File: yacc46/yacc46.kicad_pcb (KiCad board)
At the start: 2 copper layers, 281.5 x 112.1 mm, 141 parts, among them J1 CX70M-24P1, J2 OLED_I2C, J3 AVR-ISP-6, J4 GLOVE_I2C, SW1 SW_PUSH, SW10 SW_PUSH, SW11 SW_PUSH, SW12 SW_PUSH, SW13 SW_PUSH, SW14 SW_PUSH, SW15 SW_PUSH, SW16 SW_PUSH, SW17 SW_PUSH, SW18 SW_PUSH, SW19 Rotary_Encoder_Switch, SW2 SW_PUSH, SW20 SW_PUSH, SW21 SW_PUSH, SW22 SW_PUSH, SW23 SW_PUSH, SW24 SW_PUSH, SW25 SW_PUSH, SW26 SW_PUSH, SW27 SW_PUSH, SW28 SW_PUSH, SW29 SW_PUSH, SW3 SW_PUSH, SW30 SW_PUSH, SW31 SW_PUSH, SW32 SW_PUSH, SW33 SW_PUSH, SW34 SW_PUSH, SW35 SW_PUSH, SW36 Rotary_Encoder_Switch, SW37 SW_PUSH, SW38 SW_PUSH, SW39 SW_PUSH, SW4 SW_PUSH, SW40 SW_PUSH, SW41 SW_PUSH, SW42 SW_PUSH, SW43 SW_PUSH, SW44 SW_PUSH, SW45 SW_PUSH, SW46 SW_PUSH, SW47 SW_Push, SW5 SW_PUSH, SW6 SW_PUSH, SW7 SW_PUSH, SW8 SW_PUSH, SW9 SW_PUSH, U1 ATmega32U4-AU, Y1 16MHz

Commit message: GND viaを追加
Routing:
- net UDN: track 213.3 -> 212.7 mm
- net UDP: track 210.6 -> 210.1 mm
- net COL5: track 265.7 -> 266.2 mm, vias 5 -> 6
- net Net-(LED10-Pad3): vias 2 -> 4
- net GND: vias 58 -> 67

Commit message: GND, USB配線を修正
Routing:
- net SDA: track 124.9 -> 181.6 mm
- net SCL: track 124.2 -> 179.8 mm
- net VBUS: track 775.5 -> 784.1 mm, vias 0 -> 5
- net UDP: track 210.1 -> 215.4 mm
- net UDN: track 212.7 -> 218.0 mm
- net GND: track 898.8 -> 893.6 mm, vias 67 -> 159
- net COL6: track 184.9 -> 188.6 mm
- net COL5: track 266.2 -> 268.6 mm
- net COL4: track 301.0 -> 303.4 mm
- net COL3: track 356.6 -> 359.0 mm
- net COL2: track 364.9 -> 367.3 mm
- net COL1: track 382.3 -> 384.7 mm
- net COL0: track 386.4 -> 388.8 mm

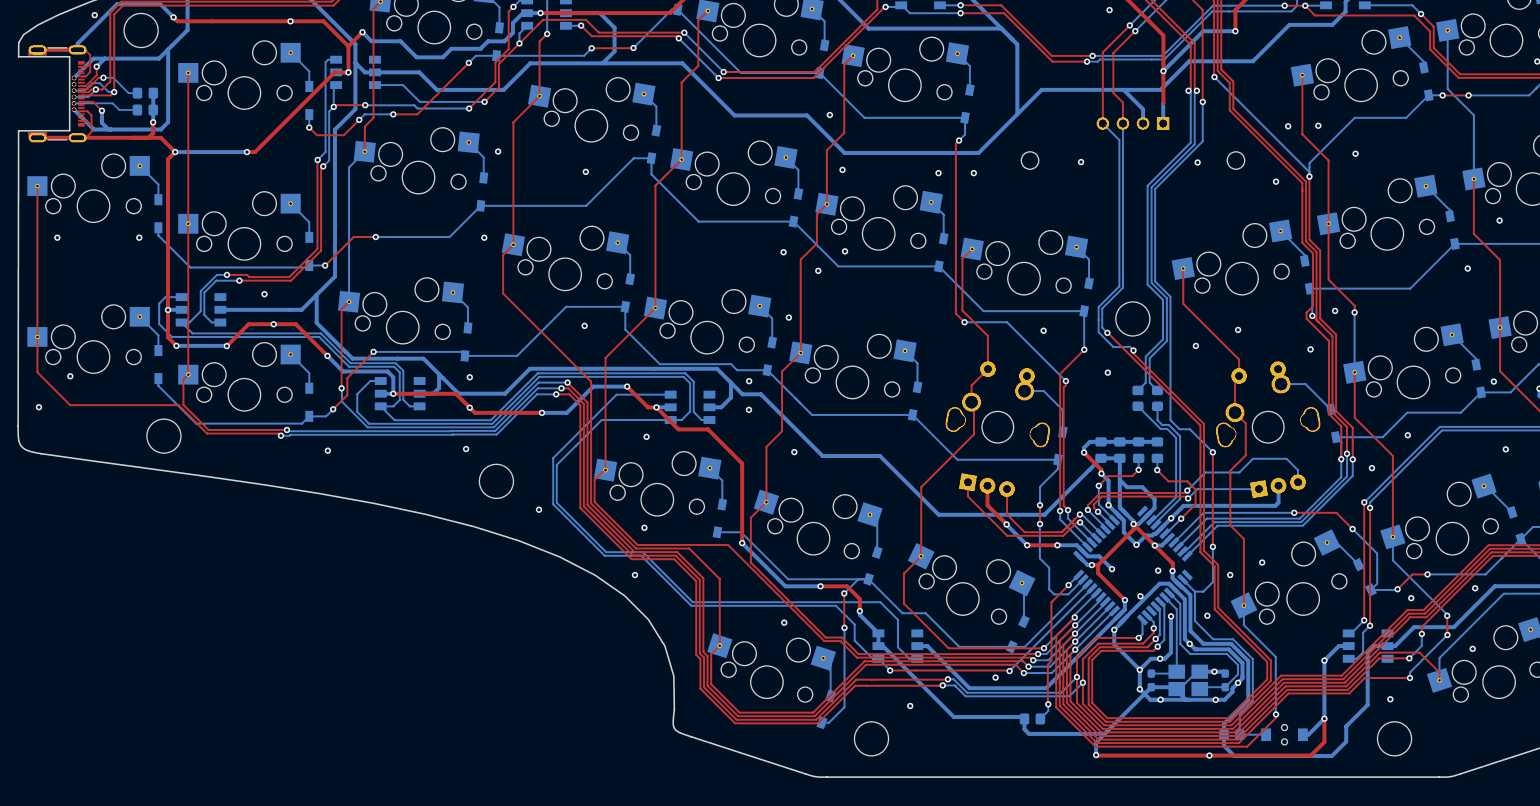
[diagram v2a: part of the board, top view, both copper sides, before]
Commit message: 基板を調整
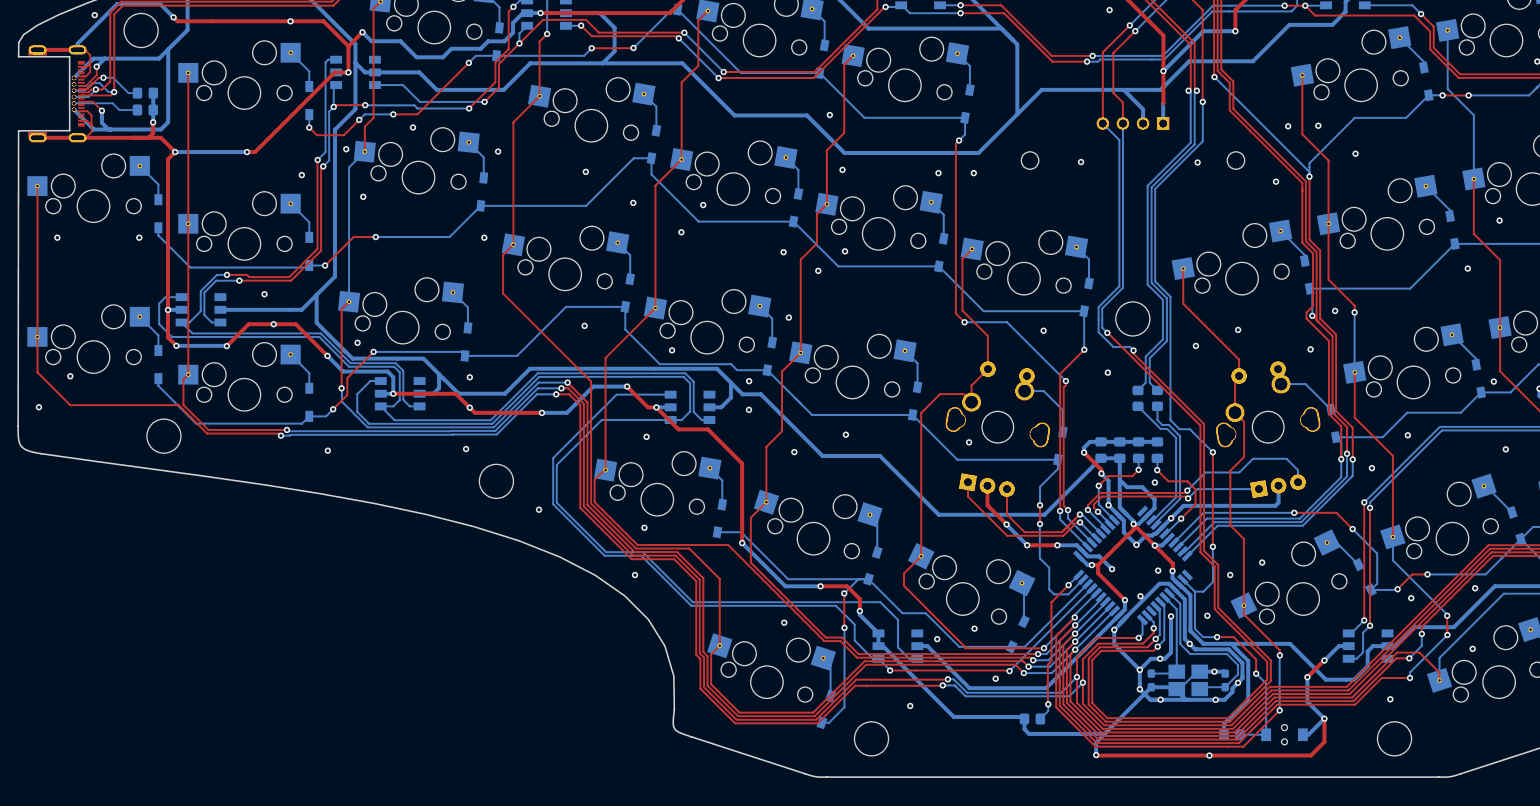
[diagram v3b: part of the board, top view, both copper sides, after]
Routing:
- net VBUS: track 784.1 -> 776.0 mm
- net COL6: track 188.6 -> 190.8 mm, vias 3 -> 4
- net GND: track 893.6 -> 895.4 mm, vias 159 -> 174
- net RESET: track 164.2 -> 165.0 mm, vias 4 -> 6
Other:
- board text added: "RESET"
- board text removed: "RST"

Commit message: v0.2発注データ
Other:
- rule pad_to_mask_clearance: 0.05 -> 0
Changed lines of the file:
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@@
     (pad_size 0.23 0.85)
     (pad_drill 0)
-    (pad_to_mask_clearance 0.05)
+    (pad_to_mask_clearance 0)
     (aux_axis_origin 0 0)
     (visible_elements 7FFFFFFF)
     (pcbplotparams
-      (layerselection 0x010fc_ffffffff)
-      (usegerberextensions false)
+      (layerselection 0x010f0_ffffffff)
+      (usegerberextensions true)
       (usegerberattributes true)
       (usegerberadvancedattributes true)
-      (creategerberjobfile true)
+      (creategerberjobfile false)
       (excludeedgelayer true)
       (linewidth 0.100000)
@@
       (outputformat 1)
       (mirror false)
-      (drillshape 1)
+      (drillshape 0)
       (scaleselection 1)
-      (outputdirectory ""))
+      (outputdirectory "garver_v0.2/"))
   )
   (net 0 "")
@@
       (effects (font (size 0.5 0.5) (thickness 0.08)) (justify mirror))
     )
-    (pad 2 smd roundrect (at 1 0) (size 1.2 1.4) (layers B.Cu B.Paste B.Mask) (roundrect_rratio 0.208333)
+    (pad 2 smd roundrect (at 1 0) (size 1.2 1.4) (layers B.Cu B.Paste B.Mask) (roundrect_rratio 0.2083325)
       (net 110 HWB))
-    (pad 1 smd roundrect (at -1 0) (size 1.2 1.4) (layers B.Cu B.Paste B.Mask) (roundrect_rratio 0.208333)
+    (pad 1 smd roundrect (at -1 0) (size 1.2 1.4) (layers B.Cu B.Paste B.Mask) (roundrect_rratio 0.2083325)
       (net 2 GND))
     (model ${KISYS3DMOD}/Resistor_SMD.3dshapes/R_0805_2012Metric.wrl
@@
       (effects (font (size 0.5 0.5) (thickness 0.08)) (justify mirror))
     )
-    (pad 2 smd roundrect (at 1 0 90) (size 1.2 1.4) (layers B.Cu B.Paste B.Mask) (roundrect_rratio 0.208333)
+    (pad 2 smd roundrect (at 1 0 90) (size 1.2 1.4) (layers B.Cu B.Paste B.Mask) (roundrect_rratio 0.2083325)
       (net 63 UDN))
-    (pad 1 smd roundrect (at -1 0 90) (size 1.2 1.4) (layers B.Cu B.Paste B.Mask) (roundrect_rratio 0.208333)
+    (pad 1 smd roundrect (at -1 0 90) (size 1.2 1.4) (layers B.Cu B.Paste B.Mask) (roundrect_rratio 0.2083325)
       (net 108 DN))
     (model ${KISYS3DMOD}/Resistor_SMD.3dshapes/R_0805_2012Metric.wrl
@@
       (effects (font (size 0.5 0.5) (thickness 0.08)) (justify mirror))
     )
-    (pad 2 smd roundrect (at 1.0375 0 270) (size 1.175 1.45) (layers B.Cu B.Paste B.Mask) (roundrect_rratio 0.212766)
+    (pad 2 smd roundrect (at 1.0375 0 270) (size 1.175 1.45) (layers B.Cu B.Paste B.Mask) (roundrect_rratio 0.2127659574468085)
       (net 1 VBUS))
-    (pad 1 smd roundrect (at -1.0375 0 270) (size 1.175 1.45) (layers B.Cu B.Paste B.Mask) (roundrect_rratio 0.212766)
+    (pad 1 smd roundrect (at -1.0375 0 270) (size 1.175 1.45) (layers B.Cu B.Paste B.Mask) (roundrect_rratio 0.2127659574468085)
       (net 2 GND))
     (model ${KISYS3DMOD}/Capacitor_SMD.3dshapes/C_0805_2012Metric.wrl
@@
       (effects (font (size 0.5 0.5) (thickness 0.08)) (justify mirror))
     )
-    (pad 1 smd roundrect (at -1.0375 0 270) (size 1.175 1.45) (layers B.Cu B.Paste B.Mask) (roundrect_rratio 0.212766)
+    (pad 1 smd roundrect (at -1.0375 0 270) (size 1.175 1.45) (layers B.Cu B.Paste B.Mask) (roundrect_rratio 0.2127659574468085)
       (net 2 GND))
-    (pad 2 smd roundrect (at 1.0375 0 270) (size 1.175 1.45) (layers B.Cu B.Paste B.Mask) (roundrect_rratio 0.212766)
+    (pad 2 smd roundrect (at 1.0375 0 270) (size 1.175 1.45) (layers B.Cu B.Paste B.Mask) (roundrect_rratio 0.2127659574468085)
       (net 1 VBUS))
     (model ${KISYS3DMOD}/Capacitor_SMD.3dshapes/C_0805_2012Metric.wrl
@@
       (effects (font (size 0.5 0.5) (thickness 0.08)) (justify mirror))
     )
-    (pad 2 smd roundrect (at 1.0375 0 90) (size 1.175 1.45) (layers B.Cu B.Paste B.Mask) (roundrect_rratio 0.212766)
+    (pad 2 smd roundrect (at 1.0375 0 90) (size 1.175 1.45) (layers B.Cu B.Paste B.Mask) (roundrect_rratio 0.2127659574468085)
       (net 2 GND))
-    (pad 1 smd roundrect (at -1.0375 0 90) (size 1.175 1.45) (layers B.Cu B.Paste B.Mask) (roundrect_rratio 0.212766)
+    (pad 1 smd roundrect (at -1.0375 0 90) (size 1.175 1.45) (layers B.Cu B.Paste B.Mask) (roundrect_rratio 0.2127659574468085)
       (net 3 AREF))
     (model ${KISYS3DMOD}/Capacitor_SMD.3dshapes/C_0805_2012Metric.wrl
@@
       (effects (font (size 0.5 0.5) (thickness 0.08)) (justify mirror))
     )
-    (pad 1 smd roundrect (at -1.0375 0 90) (size 1.175 1.45) (layers B.Cu B.Paste B.Mask) (roundrect_rratio 0.212766)
+    (pad 1 smd roundrect (at -1.0375 0 90) (size 1.175 1.45) (layers B.Cu B.Paste B.Mask) (roundrect_rratio 0.2127659574468085)
       (net 4 UCAP))
-    (pad 2 smd roundrect (at 1.0375 0 90) (size 1.175 1.45) (layers B.Cu B.Paste B.Mask) (roundrect_rratio 0.212766)
+    (pad 2 smd roundrect (at 1.0375 0 90) (size 1.175 1.45) (layers B.Cu B.Paste B.Mask) (roundrect_rratio 0.2127659574468085)
       (net 2 GND))
     (model ${KISYS3DMOD}/Capacitor_SMD.3dshapes/C_0805_2012Metric.wrl
@@
       (effects (font (size 0.5 0.5) (thickness 0.08)) (justify mirror))
     )
-    (pad 1 smd roundrect (at -1 0 180) (size 1.2 1.4) (layers B.Cu B.Paste B.Mask) (roundrect_rratio 0.208333)
+    (pad 1 smd roundrect (at -1 0 180) (size 1.2 1.4) (layers B.Cu B.Paste B.Mask) (roundrect_rratio 0.2083325)
       (net 2 GND))
-    (pad 2 smd roundrect (at 1 0 180) (size 1.2 1.4) (layers B.Cu B.Paste B.Mask) (roundrect_rratio 0.208333)
+    (pad 2 smd roundrect (at 1 0 180) (size 1.2 1.4) (layers B.Cu B.Paste B.Mask) (roundrect_rratio 0.2083325)
       (net 70 /CC1))
     (model ${KISYS3DMOD}/Resistor_SMD.3dshapes/R_0805_2012Metric.wrl
@@
       (effects (font (size 0.5 0.5) (thickness 0.08)) (justify mirror))
     )
-    (pad 2 smd roundrect (at 1 0) (size 1.2 1.4) (layers B.Cu B.Paste B.Mask) (roundrect_rratio 0.208333)
+    (pad 2 smd roundrect (at 1 0) (size 1.2 1.4) (layers B.Cu B.Paste B.Mask) (roundrect_rratio 0.2083325)
       (net 2 GND))
-    (pad 1 smd roundrect (at -1 0) (size 1.2 1.4) (layers B.Cu B.Paste B.Mask) (roundrect_rratio 0.208333)
+    (pad 1 smd roundrect (at -1 0) (size 1.2 1.4) (layers B.Cu B.Paste B.Mask) (roundrect_rratio 0.2083325)
       (net 65 /CC2))
     (model ${KISYS3DMOD}/Resistor_SMD.3dshapes/R_0805_2012Metric.wrl
@@
       (effects (font (size 0.5 0.5) (thickness 0.08)) (justify mirror))
     )
-    (pad 1 smd roundrect (at -1 0 270) (size 1.2 1.4) (layers B.Cu B.Paste B.Mask) (roundrect_rratio 0.208333)
+    (pad 1 smd roundrect (at -1 0 270) (size 1.2 1.4) (layers B.Cu B.Paste B.Mask) (roundrect_rratio 0.2083325)
       (net 64 UDP))
-    (pad 2 smd roundrect (at 1 0 270) (size 1.2 1.4) (layers B.Cu B.Paste B.Mask) (roundrect_rratio 0.208333)
+    (pad 2 smd roundrect (at 1 0 270) (size 1.2 1.4) (layers B.Cu B.Paste B.Mask) (roundrect_rratio 0.2083325)
       (net 109 DP))
     (model ${KISYS3DMOD}/Resistor_SMD.3dshapes/R_0805_2012Metric.wrl
@@
       (effects (font (size 0.5 0.5) (thickness 0.08)) (justify mirror))
     )
-    (pad 1 smd roundrect (at -1 0) (size 1.2 1.4) (layers B.Cu B.Paste B.Mask) (roundrect_rratio 0.208333)
+    (pad 1 smd roundrect (at -1 0) (size 1.2 1.4) (layers B.Cu B.Paste B.Mask) (roundrect_rratio 0.2083325)
       (net 1 VBUS))
-    (pad 2 smd roundrect (at 1 0) (size 1.2 1.4) (layers B.Cu B.Paste B.Mask) (roundrect_rratio 0.208333)
+    (pad 2 smd roundrect (at 1 0) (size 1.2 1.4) (layers B.Cu B.Paste B.Mask) (roundrect_rratio 0.2083325)
       (net 78 RESET))
     (model ${KISYS3DMOD}/Resistor_SMD.3dshapes/R_0805_2012Metric.wrl

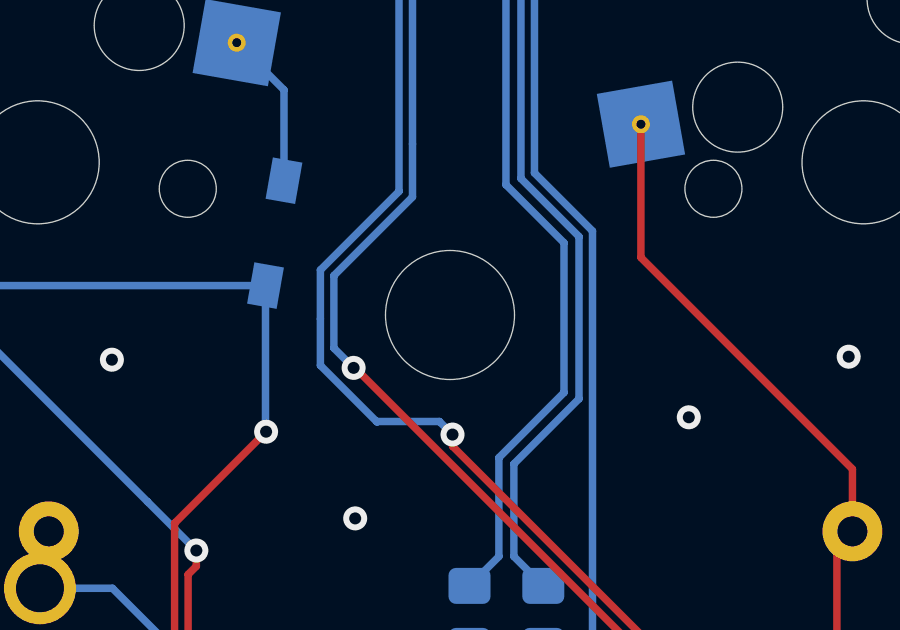
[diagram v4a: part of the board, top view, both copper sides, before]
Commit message: yacc46 PCB: MountingHoleを修正
- 中央の穴を削除
- リファレンスを修正
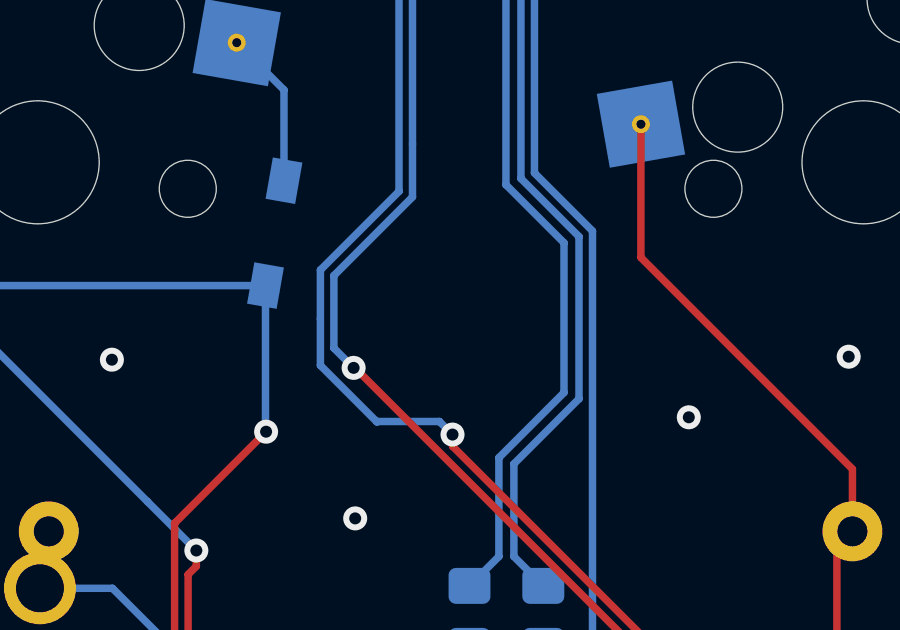
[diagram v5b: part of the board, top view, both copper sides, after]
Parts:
- removed HOLE13: Val**, foostan_kbd:M2_HOLE_v2
- renumbered HOLE1 to H1, HOLE10 to H10, HOLE11 to H11, HOLE12 to H12, HOLE14 to H13, HOLE15 to H14, HOLE2 to H2, HOLE3 to H3, HOLE4 to H4, HOLE5 to H5, HOLE6 to H6, HOLE7 to H7, HOLE8 to H8, HOLE9 to H9

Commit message: [WIP]仮配置
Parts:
- added D47: PRTR5V0U2X, 1m38_kbd:PRTR5V0U2X_SOT143B, B.Cu at (159.2, 233.9)
- added J5: GLOVE_I2C, 1m38_kbd:Grove_I2C, F.Cu at (177.7, 204.9)
- H1, H10, H11, H12, H2, H3, H4, H5, H6, H7, H8, H9: value Val** -> MountingHole
- H13, H14: value MountingHole_2.2mm_M2 -> MountingHole
- J1: value CX70M-24P1 -> USB_C_Receptacle_USB2.0; footprint digikey-footprints:USB-C_Female_CX70M-24P1 -> 1m38_kbd:USB-C_Female_CX90M-16P
- J3: value AVR-ISP-6 -> joystick_switch_joycon; footprint 1m38_kbd:ICSP-Header-ZigZag-Single -> 1m38_kbd:Molex_FPC_CON_0.5mm_5pin_5051100592
- J4: value GLOVE_I2C -> AVR-ISP-6; footprint 1m38_kbd:Grove_I2C -> 1m38_kbd:ICSP-Header-ZigZag-Single; moved to B.Cu
- LED1, LED10, LED11, LED12, LED13, LED14, LED2, LED3, LED4, LED5, LED6, LED7, LED8, LED9: value WS2813 -> WS2812B; footprint LED_SMD:LED_WS2812_PLCC6_5.0x5.0mm_P1.6mm -> foostan_kbd:LED_WS2812B-PLCC4
- moved R1 230.4 mm to (142.3, 258.2), turned to 0 degrees
- moved F1 225.8 mm to (174.9, 226.4), turned to 0 degrees
- moved R2 220.8 mm to (189.7, 216.3)
- moved J3 212.2 mm to (113.0, 239.8), turned to 0 degrees
- moved J4 203.5 mm to (129.7, 222.8), turned to 0 degrees
- moved J1 176.1 mm to (58.9, 225.7), turned to 180 degrees
- moved Y1 169.9 mm to (34.9, 226.0), turned to 0 degrees
- moved SW47 169.5 mm to (42.8, 226.2)
- moved C3 166.5 mm to (77.6, 237.9), turned to 0 degrees
- moved C1 161.5 mm to (77.6, 234.9), turned to 0 degrees
- moved R3 161.3 mm to (166.2, 251.5), turned to 0 degrees
- moved C2 157.3 mm to (127.9, 249.9), turned to 0 degrees
- moved C4 157.3 mm to (132.7, 249.9), turned to 0 degrees
- moved C6 157.1 mm to (68.4, 239.7), turned to 0 degrees
- moved C5 148.0 mm to (72.8, 239.7), turned to 0 degrees
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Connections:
- J1 pad A5: /CC1 -> Net-(J1-PadA5)
- J1 pad A8: Net-(J1-PadA8) -> (no net)
- J1 pad B5: /CC2 -> Net-(J1-PadB5)
- J1 pad B8: Net-(J1-PadB8) -> (no net)
- J3 pad 1: MISO -> JOYSTX
- J3 pad 2: VBUS -> GND
- J3 pad 3: ROWR2 -> JOYSTBT
- J3 pad 4: MOSI -> JOYSTY
- J3 pad 5: RESET -> VBUS
- J4 pad 1: SDA -> MISO
- J4 pad 2: SCL -> VBUS
- J4 pad 3: VBUS -> ROWR2
- J4 pad 4: GND -> MOSI
- LED1 pad 1: Net-(LED1-Pad1) -> VBUS
- LED1 pad 2: VBUS -> Net-(LED1-Pad2)
- LED1 pad 3: Net-(LED1-Pad3) -> GND
- LED10 pad 1: Net-(LED10-Pad1) -> VBUS
- LED10 pad 2: VBUS -> Net-(LED10-Pad2)
- LED10 pad 3: Net-(LED10-Pad3) -> GND
- LED11 pad 1: Net-(LED11-Pad1) -> VBUS
- LED11 pad 2: VBUS -> Net-(LED11-Pad2)
- LED11 pad 3: Net-(LED11-Pad3) -> GND
- LED11 pad 4: Net-(LED10-Pad3) -> Net-(LED10-Pad2)
- LED12 pad 1: Net-(LED12-Pad1) -> VBUS
- LED12 pad 2: VBUS -> Net-(LED12-Pad2)
- LED12 pad 3: Net-(LED12-Pad3) -> GND
- LED12 pad 4: Net-(LED11-Pad3) -> Net-(LED11-Pad2)
- LED13 pad 1: Net-(LED13-Pad1) -> VBUS
- LED13 pad 2: VBUS -> Net-(LED13-Pad2)
- LED13 pad 3: Net-(LED13-Pad3) -> GND
- LED13 pad 4: Net-(LED12-Pad3) -> Net-(LED12-Pad2)
- LED14 pad 1: Net-(LED14-Pad1) -> VBUS
- LED14 pad 2: VBUS -> (no net)
- LED14 pad 3: Net-(LED14-Pad3) -> GND
- LED14 pad 4: Net-(LED13-Pad3) -> Net-(LED13-Pad2)
- LED2 pad 1: Net-(LED2-Pad1) -> VBUS
- LED2 pad 2: VBUS -> Net-(LED2-Pad2)
- LED2 pad 3: Net-(LED2-Pad3) -> GND
- LED2 pad 4: Net-(LED1-Pad3) -> Net-(LED1-Pad2)
- LED3 pad 1: Net-(LED3-Pad1) -> VBUS
- LED3 pad 2: VBUS -> Net-(LED3-Pad2)
- LED3 pad 3: Net-(LED3-Pad3) -> GND
- LED3 pad 4: Net-(LED2-Pad3) -> Net-(LED2-Pad2)
- LED4 pad 1: Net-(LED4-Pad1) -> VBUS
- LED4 pad 2: VBUS -> Net-(LED4-Pad2)
- LED4 pad 3: Net-(LED4-Pad3) -> GND
- LED4 pad 4: Net-(LED3-Pad3) -> Net-(LED3-Pad2)
- LED5 pad 1: Net-(LED5-Pad1) -> VBUS
- LED5 pad 2: VBUS -> Net-(LED5-Pad2)
- LED5 pad 3: Net-(LED5-Pad3) -> GND
- LED5 pad 4: Net-(LED4-Pad3) -> Net-(LED4-Pad2)
- LED6 pad 1: Net-(LED6-Pad1) -> VBUS
- LED6 pad 2: VBUS -> Net-(LED6-Pad2)
- LED6 pad 3: Net-(LED6-Pad3) -> GND
- LED6 pad 4: Net-(LED5-Pad3) -> Net-(LED5-Pad2)
- LED7 pad 1: Net-(LED7-Pad1) -> VBUS
- LED7 pad 2: VBUS -> Net-(LED7-Pad2)
- LED7 pad 3: Net-(LED7-Pad3) -> GND
- LED7 pad 4: Net-(LED6-Pad3) -> Net-(LED6-Pad2)
- LED8 pad 1: Net-(LED8-Pad1) -> VBUS
- LED8 pad 2: VBUS -> Net-(LED8-Pad2)
- LED8 pad 3: Net-(LED10-Pad6) -> GND
- LED8 pad 4: Net-(LED7-Pad3) -> Net-(LED7-Pad2)
- LED9 pad 1: Net-(LED9-Pad1) -> VBUS
- LED9 pad 2: VBUS -> Net-(LED10-Pad4)
- LED9 pad 3: Net-(LED10-Pad4) -> GND
- LED9 pad 4: Net-(LED10-Pad6) -> Net-(LED8-Pad2)
- R1 pad 1: GND -> Net-(J1-PadA5)
- R1 pad 2: /CC1 -> GND
- R2 pad 1: /CC2 -> GND
- R2 pad 2: GND -> Net-(J1-PadB5)
- R4 pad 1: UDP -> DP
- R4 pad 2: DP -> UDP
- U1 pad 1: Net-(U1-Pad1) -> JOYSTBT
- U1 pad 12: Net-(U1-Pad12) -> ROWL0
- U1 pad 20: Net-(U1-Pad20) -> ROWL1
- U1 pad 36: ROWL1 -> ENCL1
- U1 pad 37: ROWL0 -> ENCL2
- U1 pad 38: ENCL1 -> ENCR2
- U1 pad 39: ENCL2 -> ENCR1
- U1 pad 40: ENCR2 -> JOYSTY
- U1 pad 41: ENCR1 -> JOYSTX
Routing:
- net GND: track 895.4 -> 0.00 mm, vias 174 -> 0
- net VBUS: track 776.0 -> 0.00 mm, vias 5 -> 0
- net COL0: track 388.8 -> 0.00 mm, vias 5 -> 0
- net COL1: track 384.7 -> 0.00 mm, vias 9 -> 0
- net COL2: track 367.3 -> 0.00 mm, vias 7 -> 0
- net COL3: track 359.0 -> 0.00 mm, vias 5 -> 0
- net COL4: track 303.4 -> 0.00 mm, vias 6 -> 0
- net MOSI: track 292.9 -> 0.00 mm, vias 5 -> 0
- net ROWR2: track 292.8 -> 0.00 mm, vias 4 -> 0
- net MISO: track 287.8 -> 0.00 mm, vias 9 -> 0
- net COL5: track 268.6 -> 0.00 mm, vias 6 -> 0
- net UDN: track 218.0 -> 0.00 mm, vias 2 -> 0
- net UDP: track 215.4 -> 0.00 mm, vias 2 -> 0
- net COL6: track 190.8 -> 0.00 mm, vias 4 -> 0
- net SDA: track 181.6 -> 0.00 mm, vias 4 -> 0
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- removed copper zone on B.Cu, net GND
- removed copper zone on F.Cu, net GND
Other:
- board outline removed
- net class Default: clearance 0.2 -> 0.2032
- net class Power: clearance 0.2 -> 0.2032
- rule trace_clearance: 0.2 -> 0.2032
- board text removed: "RESET"
- board text removed: "yacc46 v0.2 PCB designed by 1.038"

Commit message: 基板外形を変更
ジョイコン配置によって横幅が広がったので、ついでに基板外形を引き直した
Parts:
- added HOLE_ST: Switch_Joycon_Joystick_FPC_hole, 1m38_kbd:Switch_Joycon_Joystick_FPC_hole, F.Cu at (154.3, 132.2)
- added ST1: Switch_Joycon_Joystick, 1m38_kbd:Switch_Joycon_Joystick, F.Cu at (167.0, 120.5)
- moved J1 205.4 mm to (128.4, 32.4)
- moved J3 122.7 mm to (154.3, 124.3), turned to 180 degrees
- moved U1 122.0 mm to (167.0, 96.7), turned to 180 degrees
- moved Y1 106.0 mm to (132.8, 185.4)
- moved SW47 106.0 mm to (140.8, 185.7)
- moved C5 81.9 mm to (141.7, 195.3)
- moved C1 81.9 mm to (146.5, 190.6)
- moved C3 81.9 mm to (146.5, 193.6)
- moved C6 81.9 mm to (137.3, 195.3)
- moved C2 56.8 mm to (126.6, 193.2)
- moved C4 56.8 mm to (131.4, 193.2)
- moved R1 56.8 mm to (141.0, 201.4)
- moved R3 56.8 mm to (164.9, 194.7)
- moved R6 56.8 mm to (172.7, 200.7)
- moved J5 49.6 mm to (208.9, 166.4)
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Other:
- board outline added: 285.5 x 112.1 mm
